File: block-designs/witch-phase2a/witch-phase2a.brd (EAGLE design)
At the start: 134.6 x 99.4 mm, 13 parts, among them IC1 74LS73D, IC10 74LS08D, IC11 74LS157D, IC2 74LS08D, IC4 74LS157D, IC5 74LS73D, IC6 74LS08D, IC7 74LS73D, IC8 74LS08D, IC9 74LS73D

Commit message: added base schematic
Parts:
- removed JP5, JP9: (no value), pinhead:2X10
- added IC3: 74ALS08D, 74xx-us:SO14
- added JP2, JP3: (no value), pinhead:2X10
- moved IC11 232.6 mm to (114.9, 75.6)
- moved IC4 198.3 mm to (17.1, 76.2)
- moved IC10 98.3 mm to (77.5, 19.7), turned to 270 degrees
- moved IC8 96.6 mm to (77.5, 34.9), turned to 270 degrees
- moved IC6 94.4 mm to (77.5, 49.5), turned to 270 degrees
- moved IC9 78.0 mm to (57.1, 19.7), turned to 270 degrees
- moved IC7 76.0 mm to (57.1, 34.9), turned to 270 degrees
- moved IC5 73.7 mm to (57.1, 49.5), turned to 270 degrees
- moved IC1 5.75 mm to (57.1, 64.1)
- moved IC2 5.75 mm to (77.5, 64.1)
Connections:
- removed net CARRY0: IC1.1
- removed net CARRY1: IC5.1
- removed net CARRY2: IC7.1
- removed net CARRY3: IC9.1
- removed net ZC0: IC1.5
- removed net ZC1: IC5.5
- removed net ZC2: IC7.5
- removed net ZC3: IC9.5
- new net CARRY_COMPLETE: IC3.8, JP3.16
- new net DK_RESET: JP1.3, JP2.3
- new net N$17: IC4.12, JP1.17
- new net N$18: IC4.9, JP1.13
- new net N$19: IC4.7, JP1.9
- new net N$20: IC4.4, JP1.5
- new net N$21: IC11.12, JP2.17
- new net N$22: IC11.9, JP2.13
- new net N$23: IC11.7, JP2.9
- new net N$24: IC11.4, JP2.5
- new net N$25: IC3.3, IC3.9
- new net N$26: IC3.10, IC3.6
- new net ZCR0: IC1.1, JP2.6
- new net ZCR1: IC5.1, JP2.10
- new net ZCR2: IC7.1, JP2.14
- new net ZCR3: IC9.1, JP2.18
- new net ZCS0: IC1.5, JP1.6
- new net ZCS1: IC5.5, JP1.10
- new net ZCS2: IC7.5, JP1.14
- new net ZCS3: IC9.5, JP1.18
- net 10A_PULSES: now also JP1.4, JP2.4, JP3.4
- net CARRYDONE0: now also IC3.1
- net CARRYDONE1: now also IC3.2
- net CARRYDONE2: now also IC3.4
- net CARRYDONE3: now also IC3.5
- net CARRY_PULSES: now also JP3.12
- net GND: now also IC3.7, JP1.19, JP1.20, JP2.19, JP2.20, JP3.19, JP3.20
- net RESET: now also JP3.3
- net TRANSFER_PULSES: now also JP3.8
- net VCC: now also IC3.14, JP1.1, JP1.2, JP2.1, JP2.2, JP3.1, JP3.2
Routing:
- net N$5: track 44.2 -> 0.00 mm, vias 2 -> 0
- net N$4: track 32.5 -> 0.00 mm, vias 2 -> 0
- net N$1: track 14.7 -> 0.00 mm
- net N$2: track 14.2 -> 0.00 mm

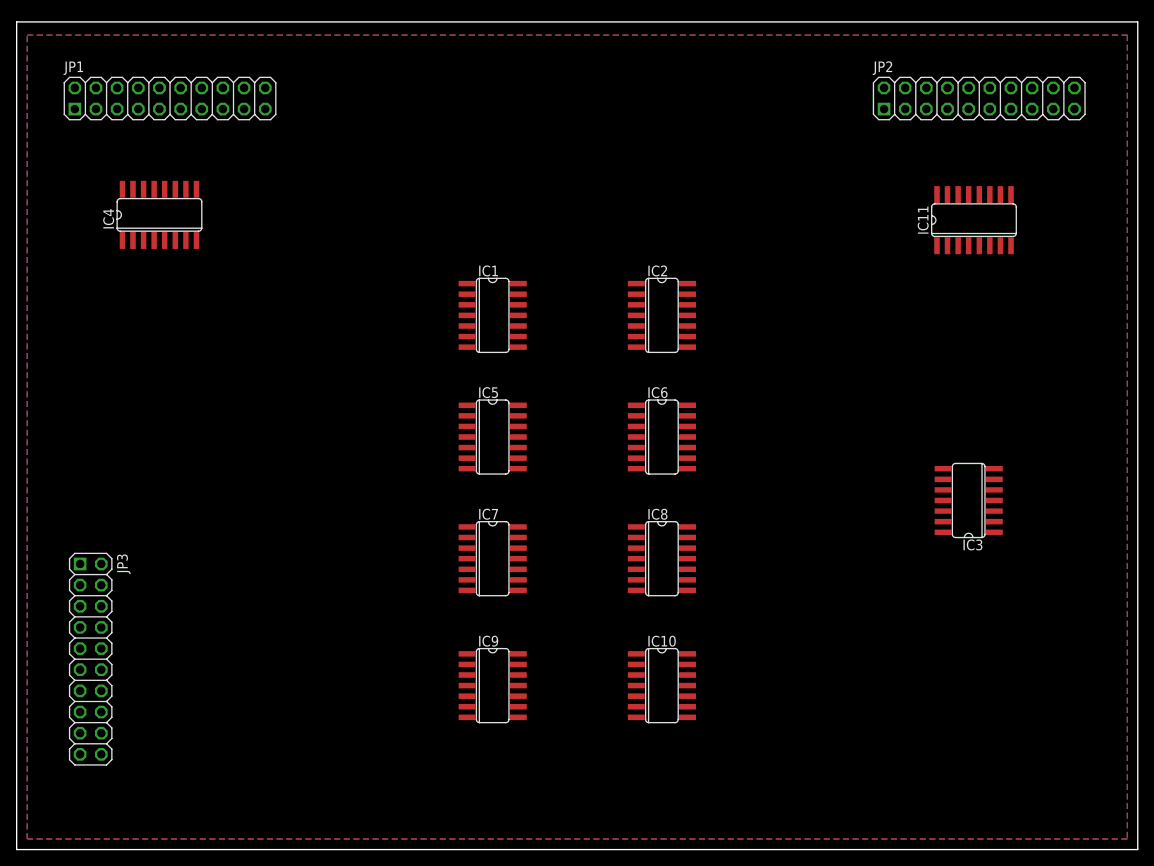
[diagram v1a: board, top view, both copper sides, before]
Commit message: routed and updated transferboard and add dekatron board
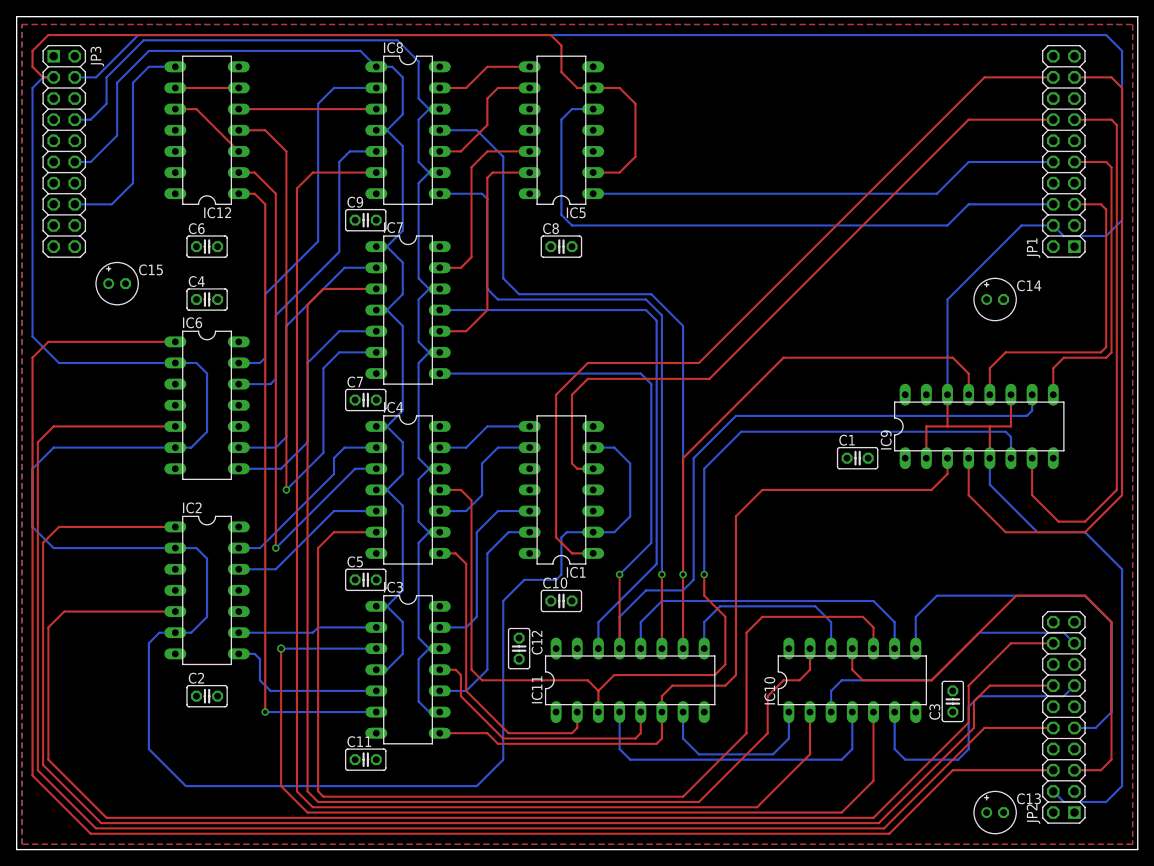
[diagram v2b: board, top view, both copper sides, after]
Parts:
- added C1, C10, C11, C12, C2, C3, C4, C5, C6, C7, C8, C9: (no value), resistor:C025-025X050
- added C13, C14, C15: (no value), resistor:E2-5
- added IC12: 74LS08N, 74xx-us:DIL14
- IC1, IC5: value 74LS73D -> 74LS73N; device 74xx-us:SO14 -> 74xx-us:DIL14
- IC10: value 74LS08D -> 74LS32N; device 74xx-us:SO14 -> 74xx-us:DIL14
- IC11: value 74LS157D -> 74LS157N; device 74xx-us:SO16 -> 74xx-us:DIL16
- IC2, IC6: value 74LS08D -> 74LS73N; device 74xx-us:SO14 -> 74xx-us:DIL14
- IC3: value 74ALS08D -> 74LS08N; device 74xx-us:SO14 -> 74xx-us:DIL14
- IC4: value 74LS157D -> 74LS08N; device 74xx-us:SO16 -> 74xx-us:DIL14
- IC7: value 74LS73D -> 74LS08N; device 74xx-us:SO14 -> 74xx-us:DIL14
- IC8: value 74LS08D -> 74LS08N; device 74xx-us:SO14 -> 74xx-us:DIL14
- IC9: value 74LS73D -> 74LS157N; device 74xx-us:SO14 -> 74xx-us:DIL16
- moved JP1 107.5 mm to (125.7, 83.8), turned to 90 degrees
- moved JP2 75.0 mm to (125.7, 15.9), turned to 90 degrees
- moved IC3 70.3 mm to (47.0, 21.6), turned to 270 degrees
- moved IC11 69.0 mm to (73.7, 20.3)
- moved IC9 66.2 mm to (115.6, 50.8), turned to 0 degrees
- moved IC2 63.8 mm to (22.9, 31.1)
- moved JP3 61.0 mm to (5.71, 83.8)
- moved IC8 59.8 mm to (47.0, 86.4)
- moved IC6 54.7 mm to (22.9, 53.3)
- moved IC4 44.5 mm to (47.0, 43.2), turned to 270 degrees
- moved IC5 37.7 mm to (65.4, 86.4), turned to 90 degrees
- moved IC7 31.5 mm to (47.0, 64.8)
- moved IC10 22.9 mm to (100.3, 20.3), turned to 0 degrees
- moved IC1 22.5 mm to (65.4, 43.2), turned to 90 degrees
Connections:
- removed net DK_RESET: JP1.3, JP2.3
- removed net N$17: IC4.12, JP1.17
- removed net N$18: IC4.9, JP1.13
- removed net N$19: IC4.7, JP1.9
- removed net N$20: IC4.4, JP1.5
- removed net N$21: IC11.12, JP2.17
- removed net N$22: IC11.9, JP2.13
- removed net N$23: IC11.7, JP2.9
- removed net N$24: IC11.4, JP2.5
- new net DKR0: IC10.3, JP2.17
- new net DKR1: IC10.6, JP2.13
- new net DKR2: IC10.8, JP2.9
- new net DKR3: IC10.11, JP2.5
- new net DKS0: IC9.4, JP1.17
- new net DKS1: IC9.7, JP1.13
- new net DKS2: IC9.9, JP1.9
- new net DKS3: IC9.12, JP1.5
- new net TRANSFEROUT0: IC10.1, IC11.7
- new net TRANSFEROUT1: IC10.4, IC11.4
- new net TRANSFEROUT2: IC10.9, IC11.12
- new net TRANSFEROUT3: IC10.12, IC11.9
- net 10A_PULSES: now also IC9.11, IC9.14, IC9.2, IC9.5; no longer IC4.11, IC4.14, IC4.2, IC4.5
- net ADD0: now also IC11.5, IC3.11; no longer IC11.2, IC2.8
- net ADD1: now also IC11.2, IC4.8; no longer IC11.5, IC6.8
- net ADD2: now also IC11.14, IC7.11; no longer IC11.11, IC8.8
- net ADD3: now also IC11.11, IC8.8; no longer IC10.8, IC11.14
- net CARRYDONE0: now also IC12.1, IC3.6; no longer IC2.3, IC3.1
- net CARRYDONE1: now also IC12.2, IC4.3; no longer IC3.2, IC6.3
- net CARRYDONE2: now also IC12.4, IC7.6; no longer IC3.4, IC8.3
- net CARRYDONE3: now also IC12.5, IC8.3; no longer IC10.3, IC3.5
- net CARRYOUT0: now also IC10.5, IC3.3; no longer IC2.6
- net CARRYOUT1: now also IC10.10, IC4.6; no longer IC6.6
- net CARRYOUT2: now also IC10.13, IC7.3; no longer IC8.6
- net CARRYOUT3: now also IC10.2, IC8.6; no longer IC10.6
- net CARRY_COMPLETE: now also IC12.8; no longer IC3.8
- net CARRY_PULSES: now also IC3.1, IC3.4, IC4.1, IC4.4, IC7.1, IC7.4, IC8.4; no longer IC10.1, IC10.5, IC2.1, IC2.5, IC6.1, IC6.5, IC8.5
- net COMP0: now also IC11.6, IC3.8, IC9.3; no longer IC11.3, IC2.11, IC4.3
- net COMP1: now also IC11.3, IC4.11, IC9.6; no longer IC11.6, IC4.6, IC6.11
- net COMP2: now also IC11.13, IC7.8, IC9.10; no longer IC11.10, IC4.10, IC8.11
- net COMP3: now also IC11.10, IC8.11, IC9.13; no longer IC10.11, IC11.13, IC4.13
- net GND: now also C1.2, C10.2, C11.2, C12.2, C13.-, C14.-, C15.-, C2.2, C3.2, C4.2, C5.2, C6.2, C7.2, C8.2, C9.2, IC12.7, IC2.10, IC2.11, IC2.3, IC4.7, IC6.10, IC6.11, IC6.3, IC7.7, IC9.8; no longer IC2.7, IC4.8, IC6.7, IC7.10, IC7.11, IC7.3, IC9.10, IC9.11, IC9.3
- net N$1: now also IC2.9, IC3.2; no longer IC1.12, IC2.4
- net N$10: now also IC5.13, IC7.10; no longer IC7.13, IC8.2
- net N$11: now also IC5.12, IC7.13; no longer IC7.9, IC8.10
- net N$12: now also IC6.9, IC7.2; no longer IC7.8, IC8.12
- net N$13: now also IC6.13, IC8.2; no longer IC10.4, IC9.12
- net N$14: now also IC5.8, IC8.13; no longer IC10.2, IC9.13
- net N$15: now also IC5.9, IC8.10; no longer IC10.10, IC9.9
- net N$16: now also IC6.12, IC8.5; no longer IC10.12, IC9.8
- net N$2: now also IC2.8, IC3.5; no longer IC1.13, IC2.2
- net N$25: now also IC12.10, IC12.3; no longer IC3.3, IC3.9
- net N$26: now also IC12.6, IC12.9; no longer IC3.10, IC3.6
- net N$3: now also IC2.12, IC4.5; no longer IC5.12, IC6.4
- net N$4: now also IC1.12, IC3.13; no longer IC1.9, IC2.10
- net N$5: now also IC1.13, IC3.10; no longer IC1.8, IC2.12
- net N$6: now also IC2.13, IC4.2; no longer IC5.13, IC6.2
- net N$7: now also IC1.8, IC4.13; no longer IC5.9, IC6.10
- net N$8: now also IC1.9, IC4.10; no longer IC5.8, IC6.12
- net N$9: now also IC6.8, IC7.5; no longer IC7.12, IC8.4
- net RESET: now also IC2.2, IC2.6, IC6.2, IC6.6; no longer IC7.2, IC7.6, IC9.2, IC9.6
- net TRANSFER_PULSES: now also IC3.12, IC3.9, IC4.12, IC4.9, IC7.12, IC7.9, IC8.12; no longer IC10.13, IC10.9, IC2.13, IC2.9, IC6.13, IC6.9, IC8.13
- net VCC: now also C1.1, C10.1, C11.1, C12.1, C13.+, C14.+, C15.+, C2.1, C3.1, C4.1, C5.1, C6.1, C7.1, C8.1, C9.1, IC12.14, IC2.4, IC2.7, IC4.14, IC6.4, IC6.7, IC9.16; no longer IC4.16, IC7.4, IC7.7, IC9.14, IC9.4, IC9.7
- net ZCR0: now also IC2.5, JP2.18; no longer IC1.1, JP2.6
- net ZCR1: now also IC2.1, JP2.14; no longer IC5.1, JP2.10
- net ZCR2: now also IC6.5, JP2.10; no longer IC7.1, JP2.14
- net ZCR3: now also IC6.1, JP2.6; no longer IC9.1, JP2.18
- net ZCS0: now also IC1.1, JP1.18; no longer IC1.5, JP1.6
- net ZCS1: now also IC1.5, JP1.14; no longer IC5.5, JP1.10
- net ZCS2: now also IC5.1, JP1.10; no longer IC7.5, JP1.14
- net ZCS3: now also IC5.5, JP1.6; no longer IC9.5, JP1.18
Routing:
- net RESET: track 0.00 -> 337.0 mm
- net 10A_PULSES: track 0.00 -> 270.6 mm
- net ZCR3: track 0.00 -> 196.7 mm
- net ZCR2: track 0.00 -> 186.5 mm
- net ZCR1: track 0.00 -> 176.2 mm
- net ZCR0: track 0.00 -> 166.7 mm
- net CARRYOUT3: track 0.00 -> 152.8 mm
- net TRANSFER_PULSES: track 0.00 -> 144.3 mm
- net COMP3: track 0.00 -> 142.8 mm, vias 0 -> 1
- net CARRY_PULSES: track 0.00 -> 140.2 mm
- net CARRYOUT2: track 0.00 -> 140.0 mm
- net COMP2: track 0.00 -> 133.3 mm, vias 0 -> 1
- net COMP1: track 0.00 -> 126.1 mm, vias 0 -> 1
- net CARRYOUT1: track 0.00 -> 123.0 mm
- net CARRYOUT0: track 0.00 -> 110.2 mm, vias 0 -> 1
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- added copper zone on layer 1, net GND
- added copper zone on layer 16, net VCC
- removed copper zone on layer 16, net VDD
- removed copper zone on layer 1, net VSS
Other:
- board size 134.6 x 99.4 mm -> 134.6 x 100 mm

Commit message: updated layouts
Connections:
- net 10A_PULSES: no longer JP1.4, JP2.4
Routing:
- net 10A_PULSES: track 270.6 -> 262.4 mm
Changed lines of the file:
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@@
 <?xml version="1.0" encoding="utf-8"?>
 <!DOCTYPE eagle SYSTEM "eagle.dtd">
-<eagle version="6.4">
+<eagle version="6.5.0">
 <drawing>
 <settings>
@@
 </signal>
 <signal name="10A_PULSES">
-<contactref element="JP2" pad="4"/>
 <contactref element="JP3" pad="4"/>
 <contactref element="IC9" pad="2"/>
@@
 <contactref element="IC9" pad="11"/>
 <contactref element="IC9" pad="14"/>
-<wire x1="6.985" y1="92.71" x2="9.525" y2="92.71" width="0.254" layer="16"/>
-<wire x1="9.525" y1="92.71" x2="14.605" y2="97.79" width="0.254" layer="16"/>
-<wire x1="14.605" y1="97.79" x2="130.81" y2="97.79" width="0.254" layer="16"/>
-<wire x1="130.81" y1="97.79" x2="132.715" y2="95.885" width="0.254" layer="16"/>
-<wire x1="132.715" y1="95.885" x2="132.715" y2="75.565" width="0.254" layer="16"/>
-<wire x1="132.715" y1="75.565" x2="130.81" y2="73.66" width="0.254" layer="16"/>
-<wire x1="124.46" y1="6.985" x2="125.73" y2="5.715" width="0.254" layer="16"/>
 <wire x1="125.73" y1="5.715" x2="130.81" y2="5.715" width="0.254" layer="16"/>
 <wire x1="130.81" y1="5.715" x2="132.715" y2="7.62" width="0.254" layer="16"/>
@@
 <wire x1="122.555" y1="38.1" x2="116.84" y2="43.815" width="0.254" layer="16"/>
 <wire x1="116.84" y1="43.815" x2="116.84" y2="46.99" width="0.254" layer="16"/>
-<wire x1="111.76" y1="54.61" x2="111.76" y2="66.04" width="0.254" layer="16"/>
-<wire x1="111.76" y1="66.04" x2="120.65" y2="74.93" width="0.254" layer="16"/>
 <wire x1="111.76" y1="54.61" x2="111.76" y2="50.8" width="0.254" layer="1"/>
 <wire x1="111.76" y1="50.8" x2="116.84" y2="50.8" width="0.254" layer="1"/>
@@
 <wire x1="109.22" y1="46.99" x2="109.22" y2="50.8" width="0.254" layer="1"/>
 <wire x1="109.22" y1="50.8" x2="111.76" y2="50.8" width="0.254" layer="1"/>
-<contactref element="JP1" pad="4"/>
-<wire x1="120.65" y1="74.93" x2="124.46" y2="74.93" width="0.254" layer="16"/>
-<wire x1="130.81" y1="73.66" x2="125.73" y2="73.66" width="0.254" layer="16"/>
-<wire x1="125.73" y1="73.66" x2="124.46" y2="74.93" width="0.254" layer="16"/>
+<wire x1="6.985" y1="92.71" x2="9.525" y2="92.71" width="0.254" layer="16"/>
+<wire x1="9.525" y1="92.71" x2="14.605" y2="97.79" width="0.254" layer="16"/>
+<wire x1="14.605" y1="97.79" x2="130.175" y2="97.79" width="0.254" layer="16"/>
+<wire x1="130.175" y1="97.79" x2="131.445" y2="96.52" width="0.254" layer="16"/>
+<wire x1="131.445" y1="96.52" x2="131.445" y2="59.69" width="0.254" layer="16"/>
+<wire x1="131.445" y1="59.69" x2="130.81" y2="59.055" width="0.254" layer="16"/>
+<wire x1="130.81" y1="59.055" x2="120.65" y2="59.055" width="0.254" layer="16"/>
+<wire x1="120.65" y1="59.055" x2="119.38" y2="57.785" width="0.254" layer="16"/>
+<wire x1="119.38" y1="57.785" x2="119.38" y2="54.61" width="0.254" layer="16"/>
 </signal>
 <signal name="ZCR0">
